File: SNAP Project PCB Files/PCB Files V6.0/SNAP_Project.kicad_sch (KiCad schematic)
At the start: 52 parts, among them IC1 ADP121-AUJZ30R7, J1 USB_C_Receptacle_USB2.0, J3 Serial Wire Debug, J4 OLED Screen Conn, Q1 2N7000, Q2 2N7000, Q3 2N7000, Q5 2N7002KDW_R1_00001, Q6 771-BSS84AK215, SW1 OS102011MA1QN1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

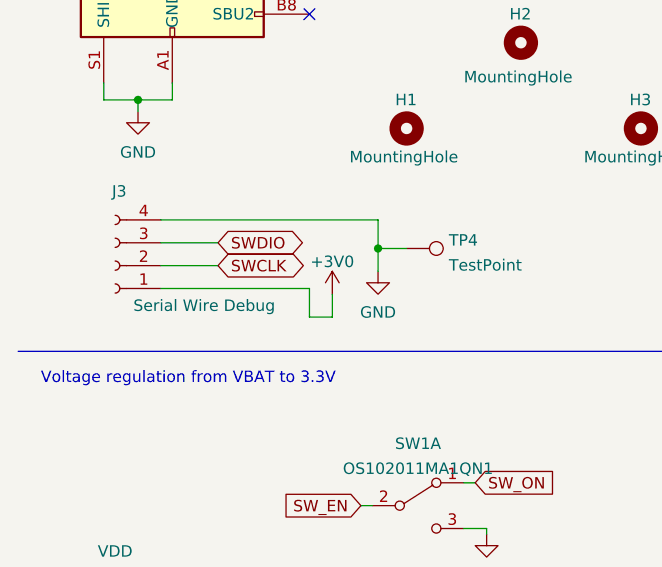
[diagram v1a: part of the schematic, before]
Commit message: OLED Screen Fix & Board corrections
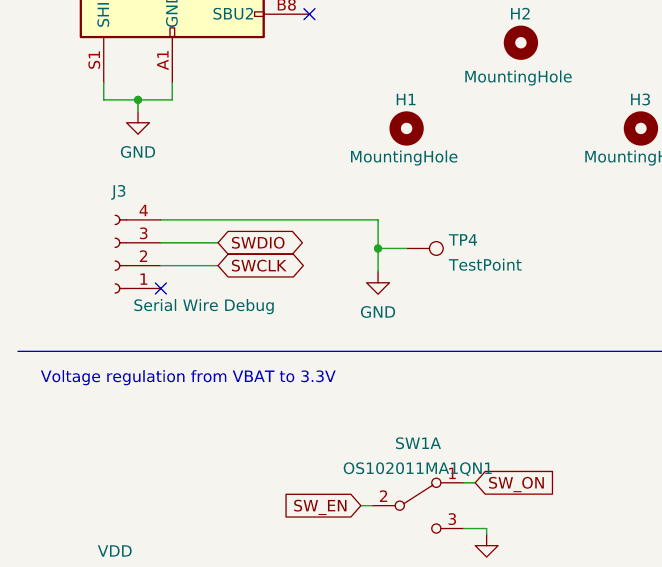
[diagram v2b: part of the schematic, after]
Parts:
- BT1: footprint Connector_Molex:Molex_PicoBlade_53047-0210_1x02_P1.25mm_Vertical -> Connector_Molex:Molex_KK-254_AE-6410-02A_1x02_P2.54mm_Vertical
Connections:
- net +3V0: no longer J3.1 (Pin_1)
- no-connect marks 3 -> 4
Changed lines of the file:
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@@
   (no_connect (at 44.45 60.96))
   (no_connect (at 145.415 182.245))
+  (no_connect (at 27.94 91.44))
   (wire (pts (xy 120.65 179.705) (xy 120.65 182.245))
     (stroke (width 0) (type default) (color 0 0 0 0))
@@
     (stroke (width 0) (type default) (color 0 0 0 0))
   )
-  (wire (pts (xy 46.99 94.615) (xy 46.99 92.075))
-    (stroke (width 0) (type default) (color 0 0 0 0))
-  )
   (wire (pts (xy 44.45 50.8) (xy 46.355 50.8))
     (stroke (width 0) (type default) (color 0 0 0 0))
@@
     (stroke (width 0) (type default) (color 0 0 0 0))
   )
-  (wire (pts (xy 44.45 91.44) (xy 44.45 94.615))
-    (stroke (width 0) (type default) (color 0 0 0 0))
-  )
   (wire (pts (xy 276.86 57.15) (xy 281.94 57.15))
     (stroke (width 0) (type default) (color 0 0 0 0))
@@
     (stroke (width 0) (type default) (color 0 0 0 0))
   )
-  (wire (pts (xy 44.45 94.615) (xy 46.99 94.615))
-    (stroke (width 0) (type default) (color 0 0 0 0))
-  )
   (wire (pts (xy 69.85 41.275) (xy 68.58 41.275))
     (stroke (width 0) (type default) (color 0 0 0 0))
@@
   )
   (wire (pts (xy 220.345 134.62) (xy 222.885 134.62))
-    (stroke (width 0) (type default) (color 0 0 0 0))
-  )
-  (wire (pts (xy 27.94 91.44) (xy 44.45 91.44))
     (stroke (width 0) (type default) (color 0 0 0 0))
   )
@@
       (effects (font (size 1.27 1.27)) (justify left))
     )
-    (property "Footprint" "Connector_Molex:Molex_PicoBlade_53047-0210_1x02_P1.25mm_Vertical" (id 2) (at 146.685 84.201 90)
+    (property "Footprint" "Connector_Molex:Molex_KK-254_AE-6410-02A_1x02_P2.54mm_Vertical" (id 2) (at 146.685 84.201 90)
       (effects (font (size 1.27 1.27)) hide)
     )
@@
     (pin "2")
   )
-  (symbol (lib_id "power:+3V0") (at 46.99 92.075 0) (unit 1)
-    (in_bom yes) (on_board yes) (fields_autoplaced)
-    (property "Reference" "#PWR08" (id 0) (at 46.99 95.885 0)
-      (effects (font (size 1.27 1.27)) hide)
-    )
-    (property "Value" "+3V0" (id 1) (at 46.99 88.4705 0))
-    (property "Footprint" "" (id 2) (at 46.99 92.075 0)
-      (effects (font (size 1.27 1.27)) hide)
-    )
-    (property "Datasheet" "" (id 3) (at 46.99 92.075 0)
-      (effects (font (size 1.27 1.27)) hide)
-    )
-    (pin "1")
-  )
   (symbol (lib_id "Device:R_Small") (at 59.055 35.56 270) (unit 1)
     (in_bom yes) (on_board yes)
@@
       (reference "#PWR07") (unit 1) (value "GND") (footprint "")
     )
-    (path "/d033157e-ae3f-4f91-b91c-5b620b61f76d"
-      (reference "#PWR08") (unit 1) (value "+3V0") (footprint "")
-    )
     (path "/9ffd6372-1837-40ec-944c-9e839fb461df/b89bffd0-89b7-4876-9b9b-6190a0ba10dd"
       (reference "#PWR09") (unit 1) (value "GND") (footprint "")
@@
     )
     (path "/2902a02f-da2d-48dc-8b69-30c550e8e97d"
-      (reference "BT1") (unit 1) (value "Battery_Cell") (footprint "Connector_Molex:Molex_PicoBlade_53047-0210_1x02_P1.25mm_Vertical")
+      (reference "BT1") (unit 1) (value "Battery_Cell") (footprint "Connector_Molex:Molex_KK-254_AE-6410-02A_1x02_P2.54mm_Vertical")
     )
     (path "/0ef1ca04-9a93-4b12-aed6-7f87933f41b3"

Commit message: New changes 1.0
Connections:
- net +3V0: now also C8.1, D2.2 (A), D3.2 (A), D4.2 (A), J4.4 (Pin_4), R15.1, R16.1, U4.5 (VDD)
- net +5V: no longer C8.1, D2.2 (A), D3.2 (A), D4.2 (A), J4.4 (Pin_4), R15.1, R16.1, U4.5 (VDD)
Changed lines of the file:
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@@
+    (pin "1")
+  )
+  (symbol (lib_id "power:+3V0") (at 233.68 111.76 0) (unit 1)
+    (in_bom yes) (on_board yes) (fields_autoplaced)
+    (property "Reference" "#PWR0119" (id 0) (at 233.68 115.57 0)
+      (effects (font (size 1.27 1.27)) hide)
+    )
+    (property "Value" "+3V0" (id 1) (at 233.68 108.1555 0))
+    (property "Footprint" "" (id 2) (at 233.68 111.76 0)
+      (effects (font (size 1.27 1.27)) hide)
+    )
+    (property "Datasheet" "" (id 3) (at 233.68 111.76 0)
+      (effects (font (size 1.27 1.27)) hide)
+    )
     (pin "1")
   )
@@
     (pin "2")
   )
-  (symbol (lib_id "power:+5V") (at 209.55 132.715 0) (unit 1)
-    (in_bom yes) (on_board yes) (fields_autoplaced)
-    (property "Reference" "#PWR022" (id 0) (at 209.55 136.525 0)
-      (effects (font (size 1.27 1.27)) hide)
-    )
-    (property "Value" "+5V" (id 1) (at 209.55 129.1105 0))
-    (property "Footprint" "" (id 2) (at 209.55 132.715 0)
-      (effects (font (size 1.27 1.27)) hide)
-    )
-    (property "Datasheet" "" (id 3) (at 209.55 132.715 0)
+  (symbol (lib_id "power:+3V0") (at 109.855 74.295 0) (unit 1)
+    (in_bom yes) (on_board yes) (fields_autoplaced)
+    (property "Reference" "#PWR0118" (id 0) (at 109.855 78.105 0)
+      (effects (font (size 1.27 1.27)) hide)
+    )
+    (property "Value" "+3V0" (id 1) (at 109.855 70.6905 0))
+    (property "Footprint" "" (id 2) (at 109.855 74.295 0)
+      (effects (font (size 1.27 1.27)) hide)
+    )
+    (property "Datasheet" "" (id 3) (at 109.855 74.295 0)
       (effects (font (size 1.27 1.27)) hide)
     )
@@
     )
     (property "Datasheet" "" (id 3) (at 75.565 145.415 0)
+      (effects (font (size 1.27 1.27)) hide)
+    )
+    (pin "1")
+  )
+  (symbol (lib_id "power:+3V0") (at 280.035 134.62 0) (unit 1)
+    (in_bom yes) (on_board yes) (fields_autoplaced)
+    (property "Reference" "#PWR0120" (id 0) (at 280.035 138.43 0)
+      (effects (font (size 1.27 1.27)) hide)
+    )
+    (property "Value" "+3V0" (id 1) (at 280.035 131.0155 0))
+    (property "Footprint" "" (id 2) (at 280.035 134.62 0)
+      (effects (font (size 1.27 1.27)) hide)
+    )
+    (property "Datasheet" "" (id 3) (at 280.035 134.62 0)
       (effects (font (size 1.27 1.27)) hide)
     )
@@
     (pin "1")
   )
-  (symbol (lib_id "power:+5V") (at 109.855 74.295 0) (unit 1)
-    (in_bom yes) (on_board yes) (fields_autoplaced)
-    (property "Reference" "#PWR0111" (id 0) (at 109.855 78.105 0)
-      (effects (font (size 1.27 1.27)) hide)
-    )
-    (property "Value" "+5V" (id 1) (at 109.855 70.6905 0))
-    (property "Footprint" "" (id 2) (at 109.855 74.295 0)
-      (effects (font (size 1.27 1.27)) hide)
-    )
-    (property "Datasheet" "" (id 3) (at 109.855 74.295 0)
-      (effects (font (size 1.27 1.27)) hide)
-    )
-    (pin "1")
-  )
   (symbol (lib_id "Mechanical:MountingHole") (at 67.945 64.135 0) (unit 1)
     (in_bom yes) (on_board yes)
@@
     (pin "1")
   )
-  (symbol (lib_id "power:+5V") (at 135.255 168.275 0) (unit 1)
-    (in_bom yes) (on_board yes) (fields_autoplaced)
-    (property "Reference" "#PWR012" (id 0) (at 135.255 172.085 0)
-      (effects (font (size 1.27 1.27)) hide)
-    )
-    (property "Value" "+5V" (id 1) (at 135.255 164.6705 0))
-    (property "Footprint" "" (id 2) (at 135.255 168.275 0)
-      (effects (font (size 1.27 1.27)) hide)
-    )
-    (property "Datasheet" "" (id 3) (at 135.255 168.275 0)
-      (effects (font (size 1.27 1.27)) hide)
-    )
-    (pin "1")
-  )
-  (symbol (lib_id "power:+5V") (at 233.68 111.76 0) (unit 1)
-    (in_bom yes) (on_board yes) (fields_autoplaced)
-    (property "Reference" "#PWR025" (id 0) (at 233.68 115.57 0)
-      (effects (font (size 1.27 1.27)) hide)
-    )
-    (property "Value" "+5V" (id 1) (at 233.68 108.1555 0))
-    (property "Footprint" "" (id 2) (at 233.68 111.76 0)
-      (effects (font (size 1.27 1.27)) hide)
-    )
-    (property "Datasheet" "" (id 3) (at 233.68 111.76 0)
-      (effects (font (size 1.27 1.27)) hide)
-    )
-    (pin "1")
-  )
   (symbol (lib_id "SamacSys_Parts:ADP121-AUJZ33R7") (at 43.18 131.445 0) (unit 1)
     (in_bom yes) (on_board yes) (fields_autoplaced)
@@
     (pin "2")
   )
+  (symbol (lib_id "power:+3V0") (at 209.55 132.715 0) (unit 1)
+    (in_bom yes) (on_board yes) (fields_autoplaced)
+    (property "Reference" "#PWR0104" (id 0) (at 209.55 136.525 0)
+      (effects (font (size 1.27 1.27)) hide)
+    )
+    (property "Value" "+3V0" (id 1) (at 209.55 129.1105 0))
+    (property "Footprint" "" (id 2) (at 209.55 132.715 0)
+      (effects (font (size 1.27 1.27)) hide)
+    )
+    (property "Datasheet" "" (id 3) (at 209.55 132.715 0)
+      (effects (font (size 1.27 1.27)) hide)
+    )
+    (pin "1")
+  )
   (symbol (lib_id "Device:R_Small") (at 59.055 35.56 270) (unit 1)
     (in_bom yes) (on_board yes)
@@
     (pin "3")
   )
+  (symbol (lib_id "power:+3V0") (at 135.255 168.275 0) (unit 1)
+    (in_bom yes) (on_board yes) (fields_autoplaced)
+    (property "Reference" "#PWR0111" (id 0) (at 135.255 172.085 0)
+      (effects (font (size 1.27 1.27)) hide)
+    )
+    (property "Value" "+3V0" (id 1) (at 135.255 164.6705 0))
+    (property "Footprint" "" (id 2) (at 135.255 168.275 0)
+      (effects (font (size 1.27 1.27)) hide)
+    )
+    (property "Datasheet" "" (id 3) (at 135.255 168.275 0)
+      (effects (font (size 1.27 1.27)) hide)
+    )
+    (pin "1")
+  )
   (symbol (lib_id "power:GND") (at 263.525 158.75 0) (unit 1)
     (in_bom yes) (on_board yes) (fields_autoplaced)
@@
     )
     (property "Datasheet" "" (id 3) (at 229.87 74.295 0)
-      (effects (font (size 1.27 1.27)) hide)
-    )
-    (pin "1")
-  )
-  (symbol (lib_id "power:+5V") (at 280.035 134.62 0) (unit 1)
-    (in_bom yes) (on_board yes) (fields_autoplaced)
-    (property "Reference" "#PWR032" (id 0) (at 280.035 138.43 0)
-      (effects (font (size 1.27 1.27)) hide)
-    )
-    (property "Value" "+5V" (id 1) (at 280.035 131.0155 0))
-    (property "Footprint" "" (id 2) (at 280.035 134.62 0)
-      (effects (font (size 1.27 1.27)) hide)
-    )
-    (property "Datasheet" "" (id 3) (at 280.035 134.62 0)
       (effects (font (size 1.27 1.27)) hide)
     )
@@
       (reference "#PWR011") (unit 1) (value "+3V0") (footprint "")
     )
-    (path "/c2cf3bcd-ef00-4445-a243-c799f68d4e04"
-      (reference "#PWR012") (unit 1) (value "+5V") (footprint "")
-    )
     (path "/9a32b158-84d7-47d3-b3e3-568a4a8e12c6"
       (reference "#PWR013") (unit 1) (value "GND") (footprint "")
@@
       (reference "#PWR021") (unit 1) (value "+3V0") (footprint "")
     )
-    (path "/34ae3a90-1069-41eb-98b7-309c022be8b2"
-      (reference "#PWR022") (unit 1) (value "+5V") (footprint "")
-    )
     (path "/bc9cb9ab-66a0-498c-bfa2-8c2d8fc07cf0"
       (reference "#PWR023") (unit 1) (value "GND") (footprint "")
@@
       (reference "#PWR024") (unit 1) (value "+3V0") (footprint "")
     )
-    (path "/c481a918-21a0-4001-98ee-597d1281a2b4"
-      (reference "#PWR025") (unit 1) (value "+5V") (footprint "")
-    )
     (path "/5626ac12-d2ed-4a19-afeb-6d2ca6a733dc"
       (reference "#PWR026") (unit 1) (value "GND") (footprint "")
@@
       (reference "#PWR030") (unit 1) (value "VDD") (footprint "")
     )
-    (path "/d92bd81c-a4ef-4905-a738-66f88d689309"
-      (reference "#PWR032") (unit 1) (value "+5V") (footprint "")
-    )
     (path "/9ffd6372-1837-40ec-944c-9e839fb461df/801f7d23-296b-4c8c-8c1a-362b7cd0e7e8"
       (reference "#PWR034") (unit 1) (value "GND") (footprint "")
@@
       (reference "#PWR0103") (unit 1) (value "+BATT") (footprint "")
     )
+    (path "/cb82d10c-44cc-48b9-b88e-28c1d88c4906"
+      (reference "#PWR0104") (unit 1) (value "+3V0") (footprint "")
+    )
     (path "/d4265251-5371-423a-be0b-550112080266"
       (reference "#PWR0105") (unit 1) (value "GND") (footprint "")
@@
       (reference "#PWR0110") (unit 1) (value "GND") (footprint "")
     )
-    (path "/58059048-d6e3-4003-847f-0e689aea144e"
-      (reference "#PWR0111") (unit 1) (value "+5V") (footprint "")
+    (path "/d36bfbd4-d469-4b19-9149-1d1e294c636b"
+      (reference "#PWR0111") (unit 1) (value "+3V0") (footprint "")
     )
     (path "/610627fb-970a-4d17-bb2f-f04da27dcfaf"
@@
       (reference "#PWR0117") (unit 1) (value "GND") (footprint "")
     )
+    (path "/36ab6b3d-b745-4130-a0e2-7bf2559d70b5"
+      (reference "#PWR0118") (unit 1) (value "+3V0") (footprint "")
+    )
+    (path "/202d5f78-ae9c-438e-9dd2-98379b2148d1"
+      (reference "#PWR0119") (unit 1) (value "+3V0") (footprint "")
+    )
+    (path "/37ed7359-18c4-4394-a3f3-6fb336c0bb27"
+      (reference "#PWR0120") (unit 1) (value "+3V0") (footprint "")
+    )
     (path "/9ffd6372-1837-40ec-944c-9e839fb461df/49bba01c-3e82-4b42-914d-bd7a3920ffbf"
       (reference "AE1") (unit 1) (value "PCB Meander Antenna") (footprint "RF_Antenna:PCB Meander Antenna")
@@
       (reference "C18") (unit 1) (value "100n") (footprint "Capacitor_SMD:C_0402_1005Metric")
     )
-    (path "/9ffd6372-1837-40ec-944c-9e839fb461df/b64301f0-1dd0-495b-bba7-a414fa6d622b"
-      (reference "C19") (unit 1) (value "6p") (footprint "Capacitor_SMD:C_0402_1005Metric")
-    )
-    (path "/9ffd6372-1837-40ec-944c-9e839fb461df/5599ade7-ebbb-4dfb-a663-7689a170fc27"
-      (reference "C20") (unit 1) (value "6p") (footprint "Capacitor_SMD:C_0402_1005Metric")
-    )
     (path "/9ffd6372-1837-40ec-944c-9e839fb461df/2a22bef2-09d0-44ce-9507-0d91509342f5"

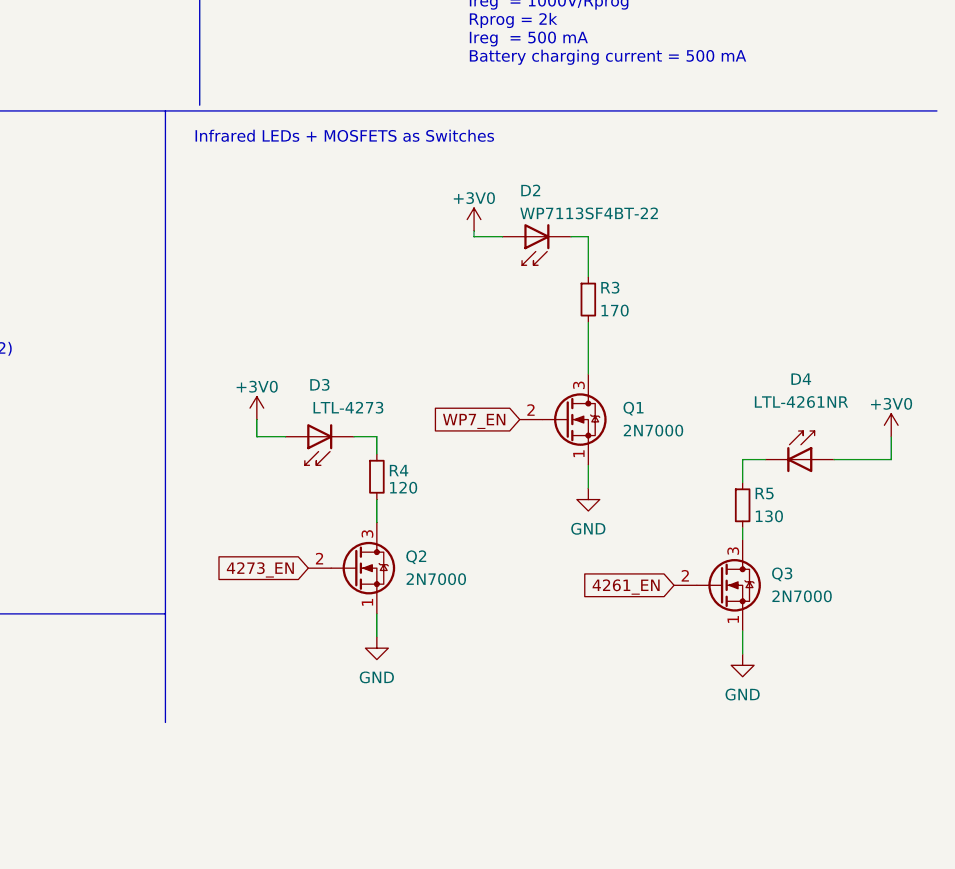
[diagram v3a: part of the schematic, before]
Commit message: Updated Connectors, LEDs, filter and STM I/O
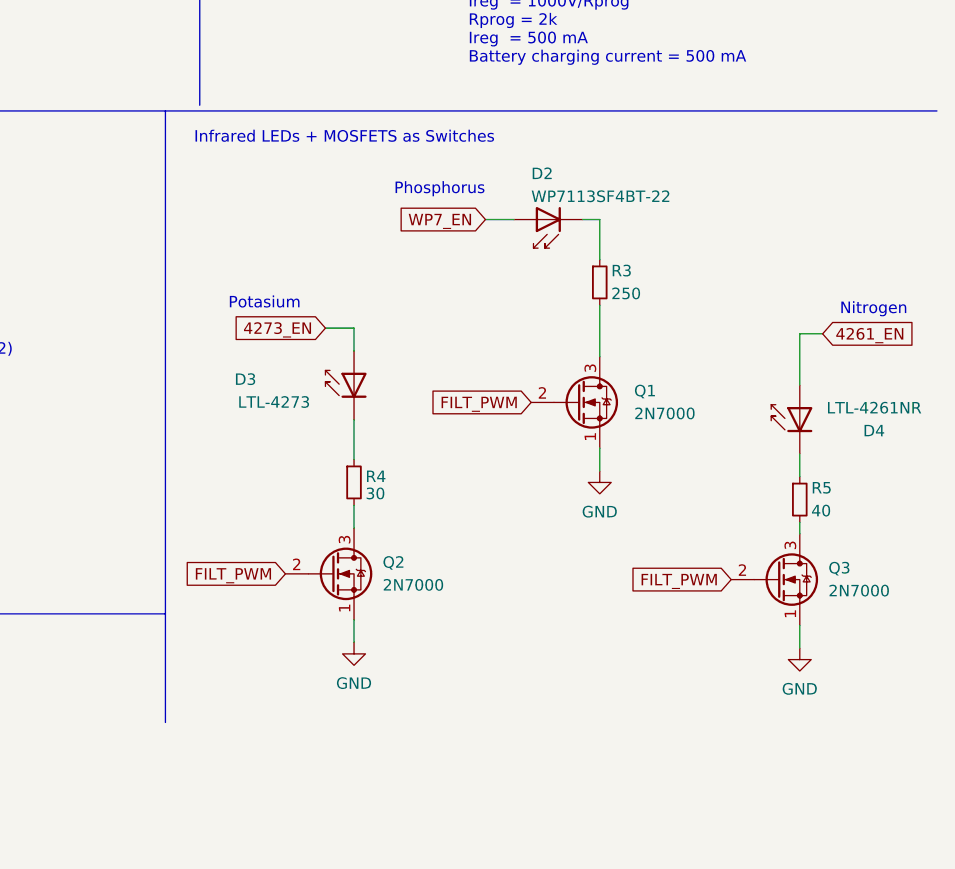
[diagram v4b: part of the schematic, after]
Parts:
- R3: value 170 -> 250
- R4: value 120 -> 30
- R5: value 130 -> 40
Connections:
- net +3V0: no longer D2.2 (A), D3.2 (A), D4.2 (A)
- net 4261_EN: now also D4.2 (A); no longer Q3.2 (G)
- net 4273_EN: now also D3.2 (A); no longer Q2.2 (G)
- net WP7_EN: now also D2.2 (A); no longer Q1.2 (G)
- new net FILT_PWM: Q1.2 (G), Q2.2 (G), Q3.2 (G)
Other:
- note added: "Nitrogen"
- note added: "Phosphorus"
- note added: "Potasium"
- moved on the sheet: D2, D3, D4, Q1, Q2, Q3, R3, R4, R5

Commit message: Last Commit before production
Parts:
- R3: footprint Resistor_SMD:R_0603_1608Metric -> Resistor_SMD:R_0805_2012Metric
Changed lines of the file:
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@@
       (effects (font (size 1.27 1.27)) (justify left))
     )
-    (property "Footprint" "Resistor_SMD:R_0603_1608Metric" (id 2) (at 247.65 117.475 0)
+    (property "Footprint" "Resistor_SMD:R_0805_2012Metric" (id 2) (at 247.65 117.475 0)
       (effects (font (size 1.27 1.27)) hide)
     )
@@
     )
     (path "/054c545c-9102-4b6e-b510-f13126e36fa9"
-      (reference "R3") (unit 1) (value "250") (footprint "Resistor_SMD:R_0603_1608Metric")
+      (reference "R3") (unit 1) (value "250") (footprint "Resistor_SMD:R_0805_2012Metric")
     )
     (path "/83fe62a8-4ef1-4faf-b1da-dad804056a3c"
